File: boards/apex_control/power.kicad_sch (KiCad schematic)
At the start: 0 parts

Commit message: Logan done fo now
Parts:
- added C1, C2, C3, C4: C, symbol APEX_Symbols:C
- added L1: L, symbol APEX_Symbols:L
- added U6: MIMXRT1171DVMAB, APEX_FOOTPRINTS:MIMXRT1171DVMAB_BGA, symbol APEX_Symbols:MIMXRT1171DVMAB
- added U7: TPS62086, APEX_FOOTPRINTS:TPS62086_RLT0007A_TI, symbol APEX_Symbols:TPS62086
- added U8: TPS62825, APEX_FOOTPRINTS:TPS62825_DMQ0006A_TI, symbol APEX_Symbols:TPS62825
- added U9: LM66200, APEX_FOOTPRINTS:LM66200_DRL0008A_TI, symbol APEX_Symbols:LM66200
- added Y1: Crystal_GND24, APEX_FOOTPRINTS:XTAL_3225, symbol APEX_Symbols:Crystal_GND24
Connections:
- new net: L1.1, U7.6 (SW)
- new net: C4.1, U6.U16 (XTALI), Y1.4 (GND)
- new net: C3.1, U6.T16 (XTALO), Y1.2 (GND)
- new net: U6.A1 (VSS), U6.A17 (VSS), U6.B7 (VSS), U6.C10 (VSS), U6.C12 (VSS), U6.C14 (VSS), U6.C8 (VSS), U6.D4 (VSS), U6.F11 (VSS), U6.F12 (VSS), U6.F13 (VSS), U6.G10 (VSS), U6.G11 (VSS), U6.G15 (VSS), U6.G3 (VSS), U6.G7 (VSS), U6.G8 (VSS), U6.G9 (VSS), U6.H11 (VSS), U6.H7 (VSS), U6.J11 (VSS), U6.J7 (VSS), U6.K11 (VSS), U6.L10 (VSS), U6.L11 (VSS), U6.L15 (VSS), U6.L3 (VSS), U6.P14 (VSS), U6.P4 (VSS), U6.R4 (VSS), U6.R7 (VSS), U6.T12 (VSS), U6.U1 (VSS), U6.U17 (VSS)
- new net: U6.H10 (VDD_SOC_IN), U6.H8 (VDD_SOC_IN), U6.H9 (VDD_SOC_IN), U6.J10 (VDD_SOC_IN), U6.J8 (VDD_SOC_IN), U6.J9 (VDD_SOC_IN), U6.K10 (VDD_SOC_IN)
- new net: U6.K6 (DCDC_GND), U6.K7 (DCDC_GND), U6.L6 (DCDC_GND)
- new net: U6.K8 (DCDC_DIG), U6.K9 (DCDC_DIG), U6.L8 (DCDC_DIG)
- new net: U6.M5 (DCDC_IN), U6.N5 (DCDC_IN)
- new net: U6.M7 (DCDC_ANA), U6.M8 (DCDC_ANA)
- new net: U6.T3 (DCDC_LP), U6.U3 (DCDC_LP)
- new net: U6.T4 (DCDC_LN), U6.U4 (DCDC_LN)
- new net +1V8: U6.D12 (NVCC_DISP1), U6.D14 (NVCC_SD1), U6.E7 (NVCC_DISP2), U6.F6 (NVCC_EMC1), U6.F7 (NVCC_EMC1), U6.G13 (NVCC_SD2), U6.G16 (ADC_VREFH), U6.G6 (NVCC_EMC1), U6.P7 (NVCC_LPSR)
- new net +3V3_1: C2.2, L1.2, U6.G12 (VDD_USB_3P3), U6.H6 (NVCC_EMC2), U6.J13 (VDDA_ADC_3P3), U6.J6 (NVCC_EMC2), U6.M12 (NVCC_GPIO), U6.R12 (VDD_LPSR_IN), U7.3 (FB), U7.4 (VOS)
- new net +5V: C1.2, U7.1 (EN), U7.7 (VIN)
- new net GND: C1.1, C2.1, C3.2, C4.2, U7.5 (GND), Y1.1, Y1.3
- no-connect marks 0 -> 1

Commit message: More placement
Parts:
- added C9: 4u7, symbol APEX_Symbols:C
- added L2: 470n, symbol APEX_Symbols:L
- C1: value C -> 10u
- C2: value C -> 22u
- L1: value L -> 470n
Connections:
- net +5V: now also U8.6 (VIN), U9.2 (VOUT), U9.7 (VOUT), C9.2
- net GND: now also U8.4 (GND), U9.1 (GND), U9.4 (~{ON}), U9.5 (GND), C9.1
- net at U8.3 (FB): now also L2.2
- net at U8.5 (SW): now also L2.1
- net VIN: now reaches U9.6 (VIN2)
- no-connect marks 1 -> 3
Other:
- moved on the sheet: C1, C2, L1, U7, U8, U9

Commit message: Tyler work
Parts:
- added C12: 1u, symbol APEX_Symbols:C
- added C13: 22u, symbol APEX_Symbols:C
- added C14: 220n, symbol APEX_Symbols:C
- added C15, C16, C19: 2.2u, symbol APEX_Symbols:C
- added C17: 100n, symbol APEX_Symbols:C
- added C18: 4.7u, symbol APEX_Symbols:C
- added R18, R19, R20, R21: 10k, symbol APEX_Symbols:R
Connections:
- net +1V8: now also L2.2, U8.3 (FB), C13.2
- net +3V3_1: now also R18.1
- net GND: now also C12.1, C13.1, C14.2, C15.2, C16.2, C17.2, C18.2, C19.2, R19.1, R20.1, R21.1
- net RC_Delay: now reaches U8.1 (EN)
- net RC_Delay: now also U6.P3 (DCDC_PSWITCH), C12.2, R18.2
- net at U6.F10 (VDD_MIPI_1P0): now also R19.2
- net at U6.F9 (VDD_MIPI_1P8): now also R20.2
- net at U6.N11 (VDDA_1P0): now also C16.1
- net at U6.N4 (DCDC_MODE): now also R21.2
- net at U6.P11 (VDD_LPSR_DIG): now also C15.1
- net at U6.P12 (VDD_LPSR_ANA): now also C18.1
- net at U6.T14 (VDD_SNVS_DIG): now also C14.1
- net at U6.U11 (NVCC_SNVS): now also U6.U14 (VDD_SNVS_ANA), C17.1, C19.1
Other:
- moved on the sheet: C9

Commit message: Worked on stuff
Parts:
- added C20, C21: 15p, symbol APEX_Symbols:C
- added L3: 4.7u, symbol APEX_Symbols:L
- added Y2: Crystal_GND24, APEX_FOOTPRINTS:XTAL_3225, symbol APEX_Symbols:Crystal_GND24
- C15, C16, C19: value 2.2u -> 2u2
- C18: value 4.7u -> 4u7
- C3, C4: value C -> 15p
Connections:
- net +3V3_1: now also U6.L5 (DCDC_IN_Q), U6.M5 (DCDC_IN), U6.N5 (DCDC_IN)
- net GND: now also U6.A1 (VSS), U6.A17 (VSS), U6.B7 (VSS), U6.C10 (VSS), U6.C12 (VSS), U6.C14 (VSS), U6.C8 (VSS), U6.D4 (VSS), U6.F11 (VSS), U6.F12 (VSS), U6.F13 (VSS), U6.G10 (VSS), U6.G11 (VSS), U6.G15 (VSS), U6.G3 (VSS), U6.G7 (VSS), U6.G8 (VSS), U6.G9 (VSS), U6.H11 (VSS), U6.H7 (VSS), U6.J11 (VSS), U6.J7 (VSS), U6.K11 (VSS), U6.K6 (DCDC_GND), U6.K7 (DCDC_GND), U6.L10 (VSS), U6.L11 (VSS), U6.L15 (VSS), U6.L3 (VSS), U6.L6 (DCDC_GND), U6.P14 (VSS), U6.P4 (VSS), U6.R4 (VSS), U6.R7 (VSS), U6.T12 (VSS), U6.U1 (VSS), U6.U17 (VSS), C20.2, C21.2, Y2.1, Y2.3
- net +V_DCDC_DIG: now reaches U6.H10 (VDD_SOC_IN), U6.H8 (VDD_SOC_IN), U6.H9 (VDD_SOC_IN), U6.J10 (VDD_SOC_IN), U6.J8 (VDD_SOC_IN), U6.J9 (VDD_SOC_IN), U6.K10 (VDD_SOC_IN)
- net +V_DCDC_DIG: now also U6.K8 (DCDC_DIG), U6.K9 (DCDC_DIG), U6.L7 (DCDC_DIG_SENSE), U6.L8 (DCDC_DIG)
- net +V_DCDC_ANA: now reaches U6.H12 (VDD_USB_1P8)
- net +V_DCDC_ANA: now also U6.K15 (VDDA_ADC_1P8), U6.M11 (VDDA_1P8_IN), U6.M6 (DCDC_ANA_SENSE), U6.M7 (DCDC_ANA), U6.M8 (DCDC_ANA)
- net at U6.T13 (RTC_XTALI): now also C20.1, Y2.2 (GND)
- net at U6.T3 (DCDC_LP), U6.U3 (DCDC_LP): now also L3.2
- net at U6.T4 (DCDC_LN), U6.U4 (DCDC_LN): now also L3.1
- net at U6.U13 (RTC_XTALO): now also C21.1, Y2.4 (GND)
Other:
- moved on the sheet: C1, C12, C13, C14, C15, C16, C17, C18, C19, C2, C3, C4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

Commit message: Worked on stuff
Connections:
- net +V_USB: now reaches U9.3 (VIN1)
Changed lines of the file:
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@@
 		(in_pos_files yes)
 		(dnp no)
-		(fields_autoplaced yes)
 		(property "Reference" "U6"
-			(at 126.746 56.896 0)
+			(at 173.99 158.242 0)
 			(show_name no)
 			(do_not_autoplace no)
@@
 		)
 		(property "Value" "MIMXRT1171DVMAB"
-			(at 126.238 54.356 0)
+			(at 166.37 155.956 0)
 			(show_name no)
 			(do_not_autoplace no)
@@
 					(unit 1)
 				)
+			)
+		)
+	)
+	(symbol
+		(lib_id "APEX_Symbols:+V_USB")
+		(at 234.95 55.88 0)
+		(unit 1)
+		(body_style 1)
+		(exclude_from_sim no)
+		(in_bom no)
+		(on_board no)
+		(in_pos_files yes)
+		(dnp no)
+		(fields_autoplaced yes)
+		(property "Reference" "#PWR057"
+			(at 235.458 66.802 0)
+			(hide yes)
+			(show_name no)
+			(do_not_autoplace no)
+			(effects
+				(font
+					(size 1.27 1.27)
+				)
+			)
+		)
+		(property "Value" "+V_USB"
+			(at 234.95 54.61 0)
+			(show_name no)
+			(do_not_autoplace no)
+			(effects
+				(font
+					(size 1.27 1.27)
+				)
+			)
+		)
+		(property "Footprint" ""
+			(at 234.95 55.88 0)
+			(hide yes)
+			(show_name no)
+			(do_not_autoplace no)
+			(effects
+				(font
+					(size 1.27 1.27)
+				)
+			)
+		)
+		(property "Datasheet" ""
+			(at 234.95 55.88 0)
+			(hide yes)
+			(show_name no)
+			(do_not_autoplace no)
+			(effects
+				(font
+					(size 1.27 1.27)
+				)
+			)
+		)
+		(property "Description" "Power symbol creates a global label with name \"+V_USB\": 5.0V USB Output"
+			(at 234.95 55.88 0)
+			(hide yes)
+			(show_name no)
+			(do_not_autoplace no)
+			(effects
+				(font
+					(size 1.27 1.27)
+				)
+			)
+		)
+		(pin "1"
+		)
+		(instances
+			(project "apex-control-2026"
+				(path "/e82f86d1-bc15-466a-bf95-b7a389511473/13918ba5-4081-4683-bd12-f7e6e14bb50f"
+					(reference "#PWR057")
+					(unit 1)
+				)

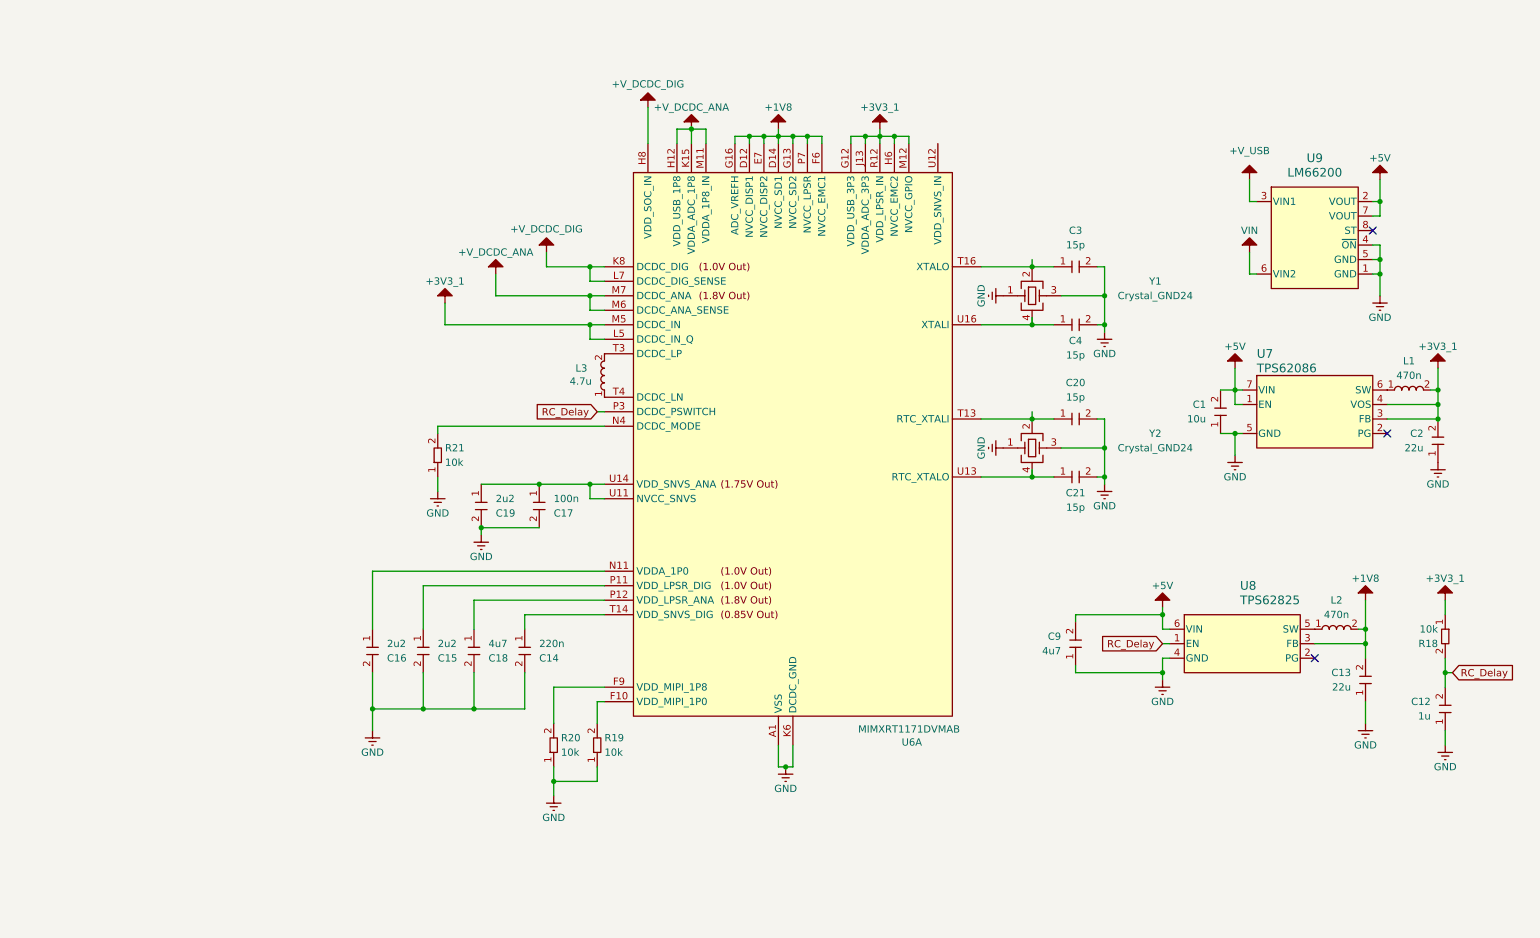
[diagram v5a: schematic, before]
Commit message: Power schematic decoupling
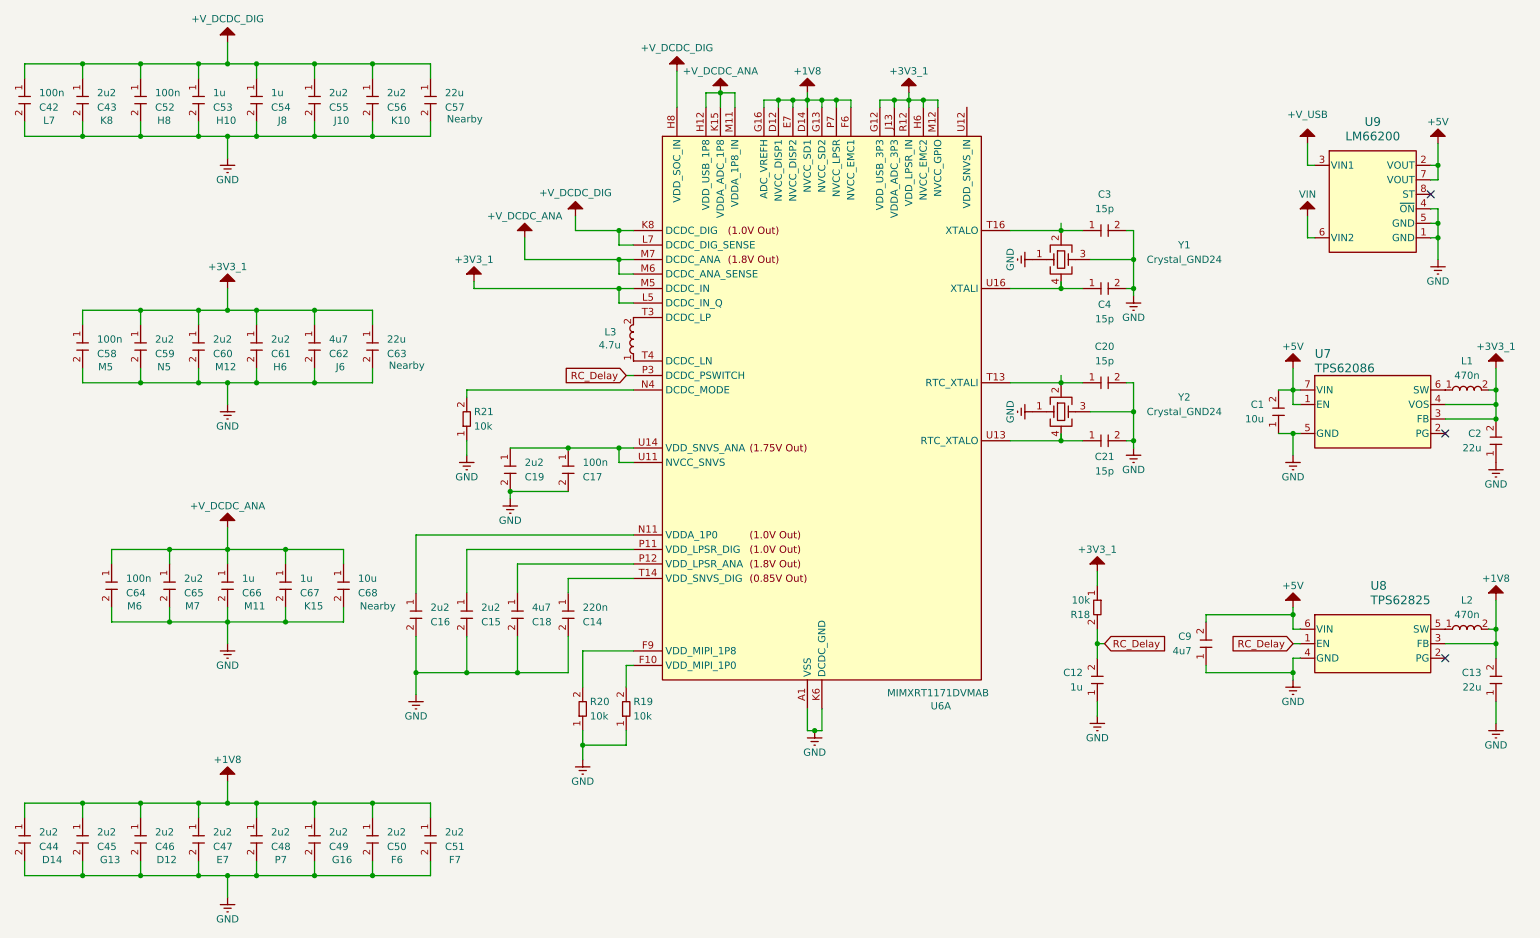
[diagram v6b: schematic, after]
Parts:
- added C42, C52, C58, C64: 100n, symbol APEX_Symbols:C
- added C43, C44, C45, C46, C47, C48, C49, C50, C51, C55, C56, C59, C60, C61, C65: 2u2, symbol APEX_Symbols:C
- added C53, C54, C66, C67: 1u, symbol APEX_Symbols:C
- added C57, C63: 22u, symbol APEX_Symbols:C
- added C62: 4u7, symbol APEX_Symbols:C
- added C68: 10u, symbol APEX_Symbols:C
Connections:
- net +1V8: now also C44.1, C45.1, C46.1, C47.1, C48.1, C49.1, C50.1, C51.1
- net +3V3_1: now also C58.1, C59.1, C60.1, C61.1, C62.1, C63.1
- net +V_DCDC_ANA: now also C64.1, C65.1, C66.1, C67.1, C68.1
- net +V_DCDC_DIG: now also C42.1, C43.1, C52.1, C53.1, C54.1, C55.1, C56.1, C57.1
- net GND: now also C42.2, C43.2, C44.2, C45.2, C46.2, C47.2, C48.2, C49.2, C50.2, C51.2, C52.2, C53.2, C54.2, C55.2, C56.2, C57.2, C58.2, C59.2, C60.2, C61.2, C62.2, C63.2, C64.2, C65.2, C66.2, C67.2, C68.2
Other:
- moved on the sheet: C1, C12, C13, C14, C15, C16, C17, C18, C19, C2, C20, C21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
